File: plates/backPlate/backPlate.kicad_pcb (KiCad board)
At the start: 2 copper layers, 242.9 x 101.2 mm, 13 parts

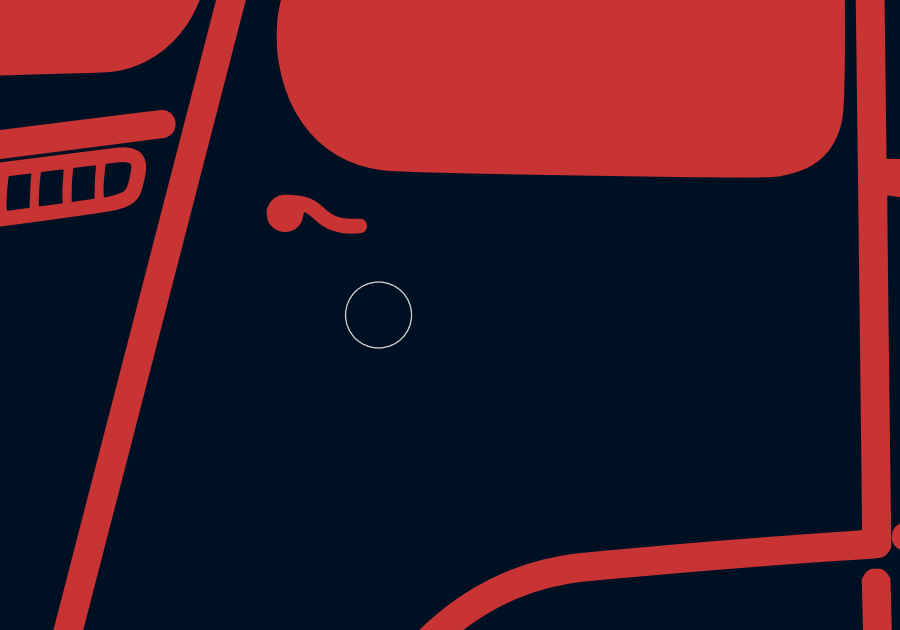
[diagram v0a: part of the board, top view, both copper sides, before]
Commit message: 🐛 Fix back plate center hole position
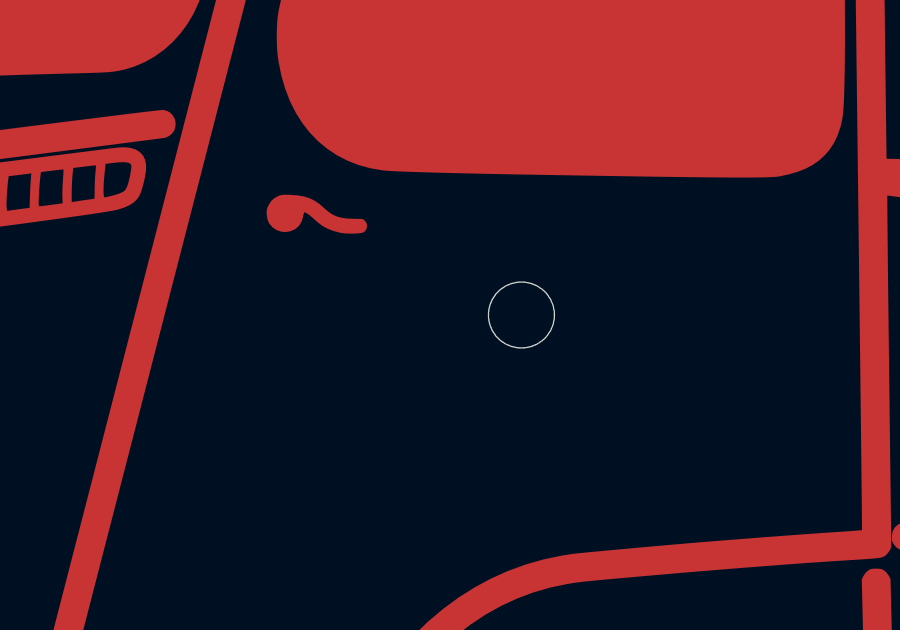
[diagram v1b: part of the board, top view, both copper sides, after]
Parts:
- moved REF** 4.76 mm to (153.2, 73.0)
